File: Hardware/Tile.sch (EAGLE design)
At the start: 1 part

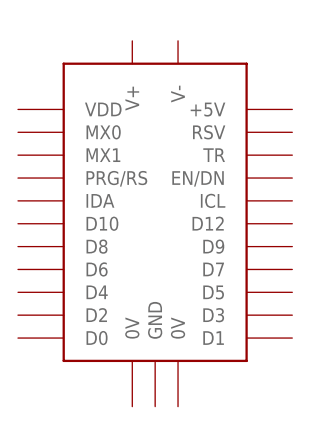
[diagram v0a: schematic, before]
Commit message: Updated tile schematic and dimensions
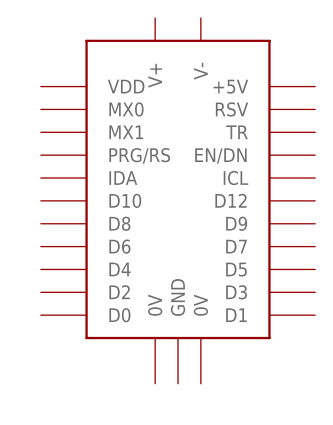
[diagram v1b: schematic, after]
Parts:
- removed U$1: UTILE_LPCARRIER_SMD_MALE_1.27, amino:UTILE_LPCARRIER_SMD_MALE_1.27
- added T1: UTILE_LPTILE, amino:UTILE_LPTILE
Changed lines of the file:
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@@
 <grid distance="0.1" unitdist="inch" unit="inch" style="lines" multiple="1" display="no" altdistance="0.01" altunitdist="inch" altunit="inch"/>
 <layers>
-<layer number="1" name="Top" color="4" fill="1" visible="no" active="no"/>
+<layer number="1" name="Top" color="29" fill="1" visible="no" active="no"/>
 <layer number="2" name="Route2" color="1" fill="3" visible="no" active="no"/>
 <layer number="3" name="Route3" color="4" fill="3" visible="no" active="no"/>
@@
 <layer number="89" name="SimProbes" color="9" fill="1" visible="yes" active="yes"/>
 <layer number="90" name="Modules" color="5" fill="1" visible="yes" active="yes"/>
-<layer number="91" name="Nets" color="2" fill="1" visible="yes" active="yes"/>
+<layer number="91" name="Nets" color="30" fill="1" visible="yes" active="yes"/>
 <layer number="92" name="Busses" color="1" fill="1" visible="yes" active="yes"/>
 <layer number="93" name="Pins" color="2" fill="1" visible="no" active="yes"/>
-<layer number="94" name="Symbols" color="4" fill="1" visible="yes" active="yes"/>
+<layer number="94" name="Symbols" color="31" fill="1" visible="yes" active="yes"/>
 <layer number="95" name="Names" color="7" fill="1" visible="yes" active="yes"/>
 <layer number="96" name="Values" color="7" fill="1" visible="yes" active="yes"/>
@@
 </classes>
 <parts>
-<part name="U$1" library="amino" deviceset="UTILE_LP" device="CARRIER_SMD_MALE_1.27"/>
+<part name="T1" library="amino" deviceset="UTILE_LP" device="TILE"/>
 </parts>
 <sheets>
@@
 </plain>
 <instances>
-<instance part="U$1" gate="G$1" x="27.94" y="33.02"/>
+<instance part="T1" gate="G$1" x="30.48" y="35.56"/>
 </instances>
 <busses>
